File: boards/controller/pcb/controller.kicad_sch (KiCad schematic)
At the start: 0 parts

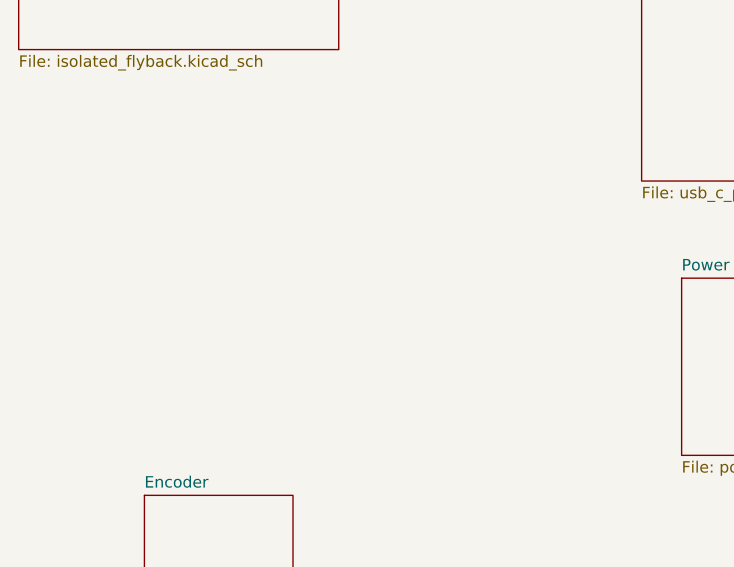
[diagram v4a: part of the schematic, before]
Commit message: controller: pcb: Update schematic
Signed-off-by: Nicholas Loehrke <nicholasnloehrke@gmail.com>
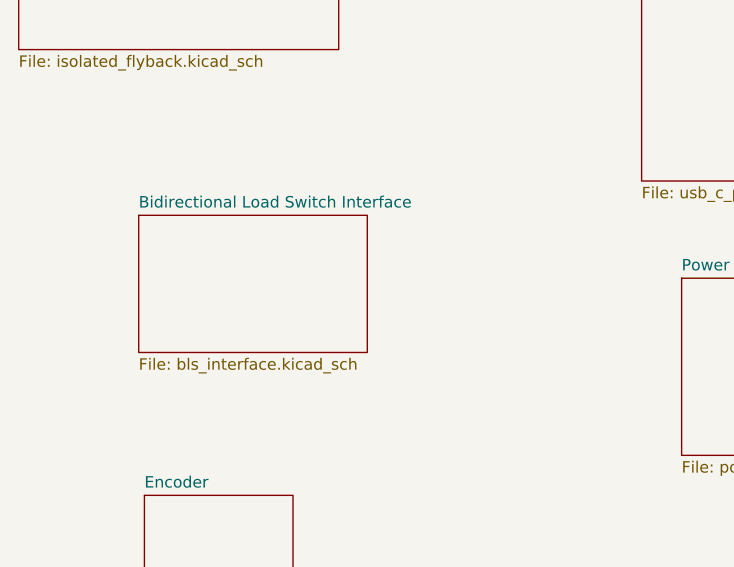
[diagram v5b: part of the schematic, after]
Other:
- added sheet Bidirectional Load Switch Interface (bls_interface.kicad_sch)
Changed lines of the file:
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@@
+	)
+	(sheet
+		(at 38.735 71.755)
+		(size 25.4 15.24)
+		(exclude_from_sim no)
+		(in_bom yes)
+		(on_board yes)
+		(dnp no)
+		(fields_autoplaced yes)
+		(stroke
+			(width 0.1524)
+			(type solid)
+		)
+		(fill
+			(color 0 0 0 0.0000)
+		)
+		(property "Sheetname" "Bidirectional Load Switch Interface"
+			(at 38.735 71.0434 0)
+			(effects
+				(font
+					(size 1.27 1.27)
+				)
+				(justify left bottom)
+			)
+		)
+		(property "Sheetfile" "bls_interface.kicad_sch"
+			(at 38.735 87.5796 0)
+			(effects
+				(font
+					(size 1.27 1.27)
+				)
+				(justify left top)
+			)
+		)
+		(instances
+			(project "controller"
+				(path "/5caba13a-97ae-46d4-856f-900b12012fd8"
+					(page "11")
+				)
+			)
+		)
 	)
 	(sheet

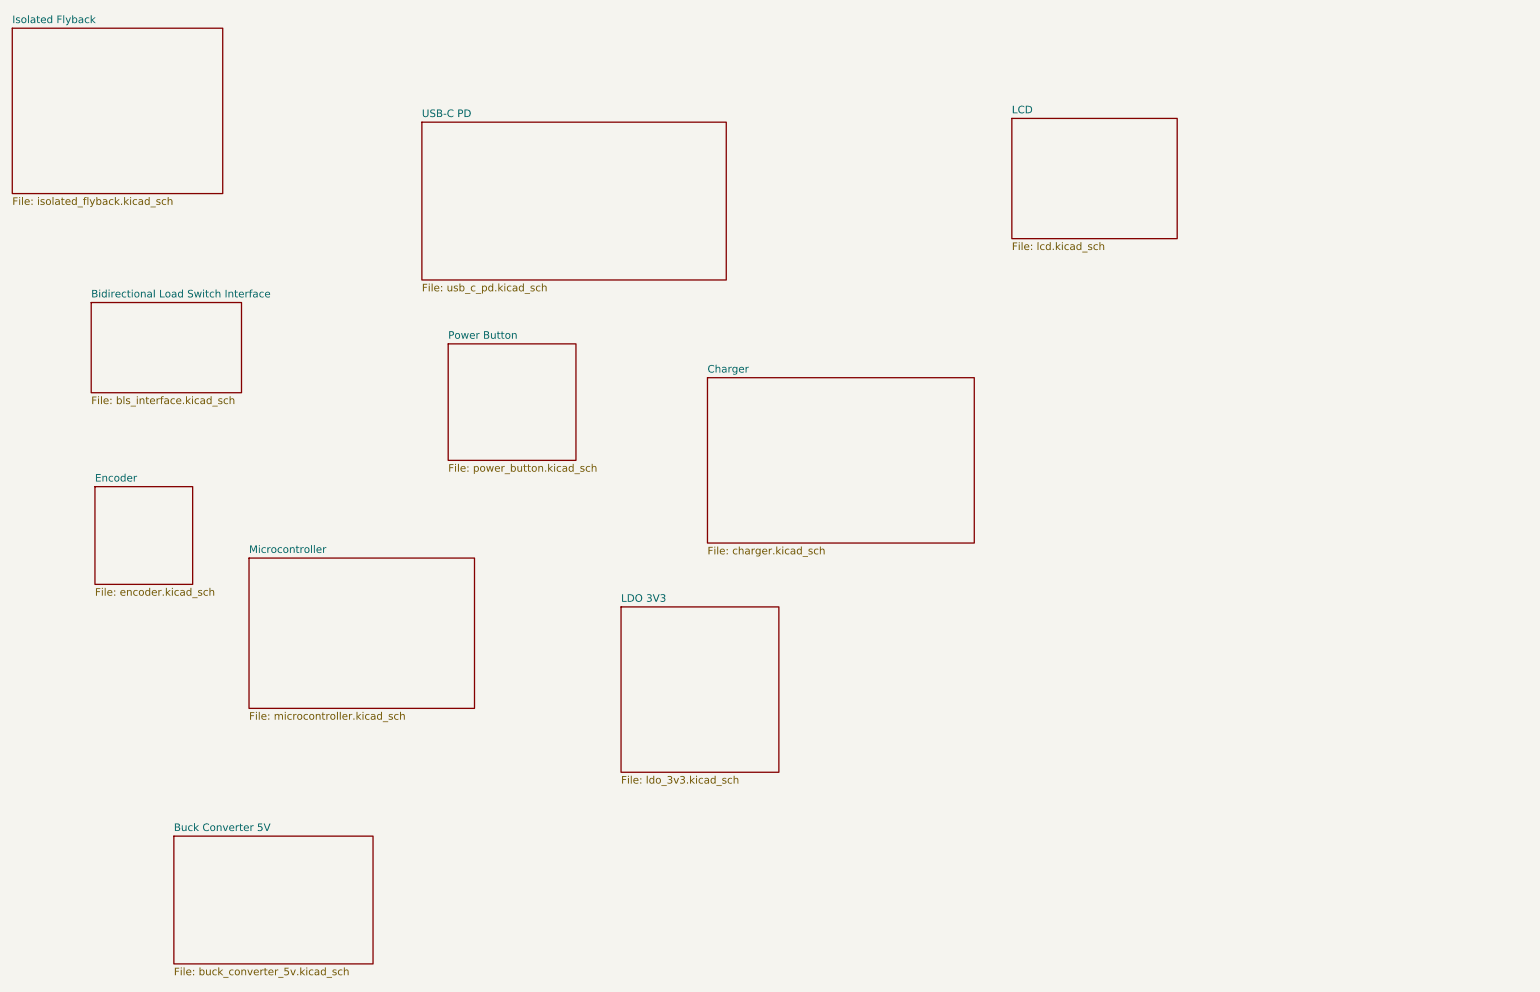
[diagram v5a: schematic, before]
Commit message: controller: pcb: Update schematic
Signed-off-by: Nicholas Loehrke <nicholasnloehrke@gmail.com>
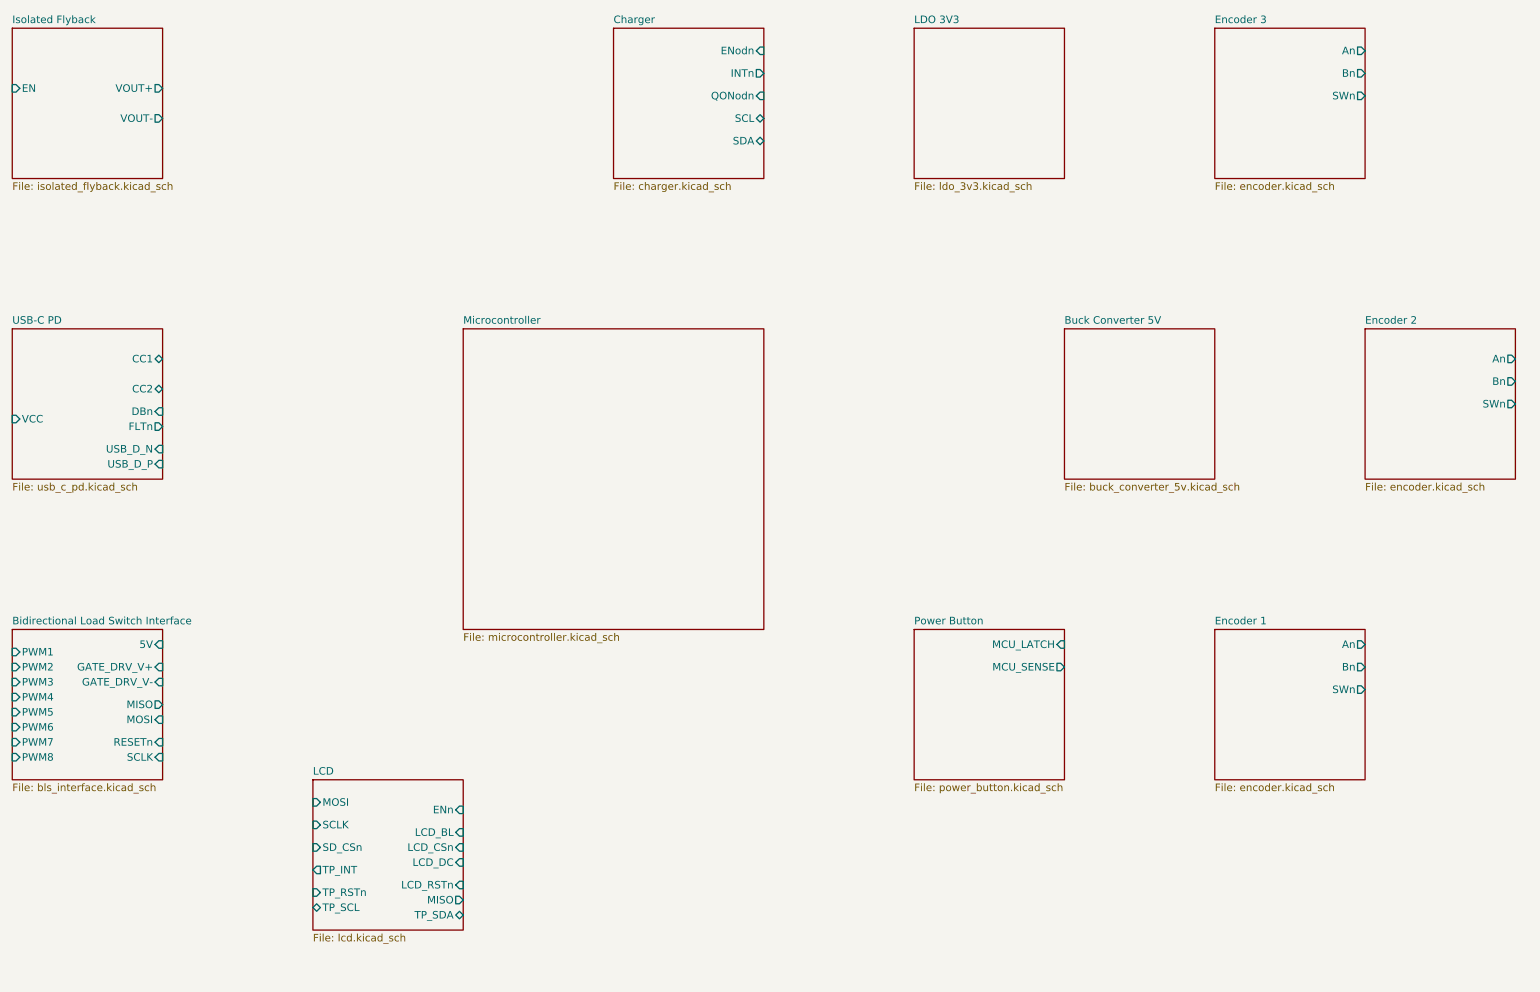
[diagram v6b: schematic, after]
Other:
- sheet Encoder renamed Encoder 1
- added sheet Encoder 2 (encoder.kicad_sch)
- added sheet Encoder 3 (encoder.kicad_sch)
- sheet Bidirectional Load Switch Interface ports: added 5V, GATE_DRV_V+, GATE_DRV_V-, MISO, MOSI, PWM1, PWM2, PWM3, PWM4, PWM5, PWM6, PWM7, PWM8, RESETn, SCLK; removed none
- sheet Charger ports: added ENodn, INTn, QONodn, SCL, SDA; removed none
- sheet Encoder 1 ports: added An, Bn, SWn; removed none
- sheet Isolated Flyback ports: added EN, VOUT+, VOUT-; removed none
- sheet LCD ports: added ENn, LCD_BL, LCD_CSn, LCD_DC, LCD_RSTn, MISO, MOSI, SCLK, SD_CSn, TP_INT, TP_RSTn, TP_SCL, TP_SDA; removed none
- sheet Power Button ports: added MCU_LATCH, MCU_SENSE; removed none
- sheet USB-C PD ports: added CC1, CC2, DBn, FLTn, USB_D_N, USB_D_P, VCC; removed none

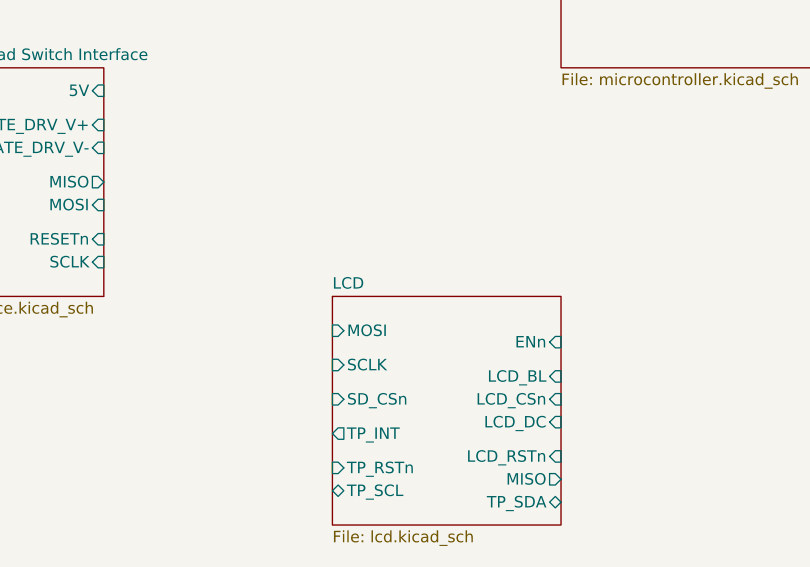
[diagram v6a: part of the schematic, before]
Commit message: controller: pcb: Update schematic
- add VBAT sense circuit
- add BLS power pmos
- assign BLS GPIO

Signed-off-by: Nicholas Loehrke <nicholasnloehrke@gmail.com>
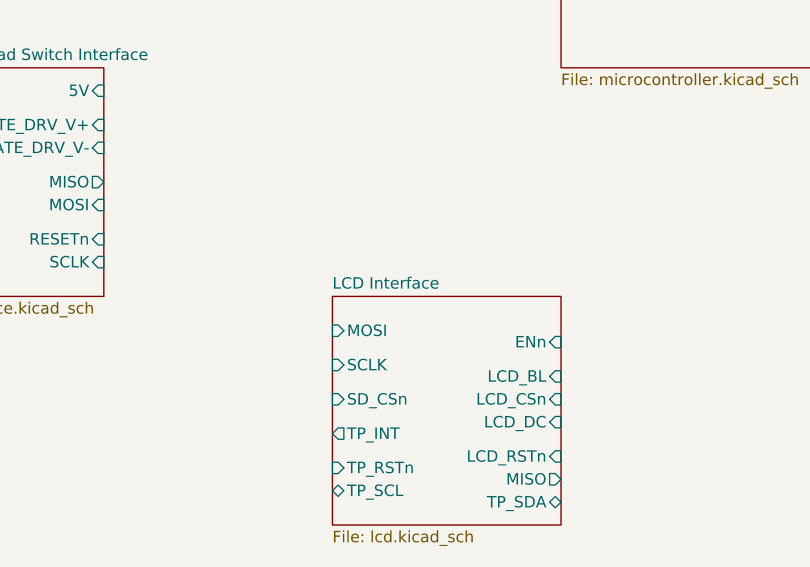
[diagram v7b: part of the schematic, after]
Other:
- sheet LCD renamed LCD Interface
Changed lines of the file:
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@@
 			(color 0 0 0 0.0000)
 		)
-		(property "Sheetname" "LCD"
+		(property "Sheetname" "LCD Interface"
 			(at 76.2 151.6884 0)
 			(effects

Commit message: controller: pcb: Update schematic
Signed-off-by: Nicholas Loehrke <nicholasnloehrke@gmail.com>
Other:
- sheet Bidirectional Load Switch Interface ports: added none; removed 5V, RESETn
- sheet Charger ports: added none; removed ENodn, QONodn
- sheet Isolated Flyback ports: added none; removed VOUT+, VOUT-
- sheet LCD Interface ports: added none; removed TP_INT
- sheet Microcontroller ports: added BLS_CH1, BLS_CH2, BLS_CH3, BLS_CH4, BLS_CH5, BLS_CH6, BLS_CH7, BLS_CH8, BLS_ENn, BLS_MISO, BLS_MOSI, BLS_RSTn, BLS_SCLK, CHG_ENn, CHG_INTn, CHG_SCL, CHG_SDA, DISP_ENn, DISP_MISO, DISP_MOSI, DISP_SCLK, ENC_1An, ENC_1Bn, ENC_2An, ENC_2Bn, ENC_3An, ENC_3Bn, LCD_BL, LCD_CSn, LCD_DC, LCD_RSTn, SD_CSn, SWCLK, SWDIO, TP_INTn, TP_RSTn, TP_SCL, TP_SDA, USART2_RX, USART2_TX, USB_CC1, USB_CC2, USB_D_N, USB_D_P, VBAT_SENSE, VBAT_SENSE_EN; removed none
- sheet Power Button ports: added none; removed MCU_SENSE
